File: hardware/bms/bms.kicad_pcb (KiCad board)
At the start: 4 copper layers, 120 x 45 mm, 265 parts, among them J1 Screw_Terminal_01x01, J10 Conn_01x10, J11 USB_C_Receptacle_USB2.0, J12 Conn_01x03, J13 Conn_01x07, J2 Screw_Terminal_01x01, J3 Screw_Terminal_01x01, J4 Screw_Terminal_01x01, J5 Screw_Terminal_01x01, J6 Conn_01x02, J7 Conn_01x10, J8 Conn_01x02, Q1 MMBT3904, Q2 Q_PMOS_GSD, Q3 Q_PMOS_GSD, Q4 BSZ018N04LS6ATMA1, Q5 IAUC120N04S6N006ATMA1, Q6 IAUC120N04S6N006ATMA1, Q7 BSZ018N04LS6ATMA1, Q8 BSZ018N04LS6ATMA1, Q9 BSZ018N04LS6ATMA1, SW1 SW_SPST, SW2 SW_Push, SW3 SW_Push, U1 BQ76952, U2 LM74700, U3 BQ24610, U4 LM5166X, U5 TPS62172DSG, U6 ESP32-C3-MINI-1-N4, U7 SN74LXC1T14DCKR, U8 USBLC6-2SC6

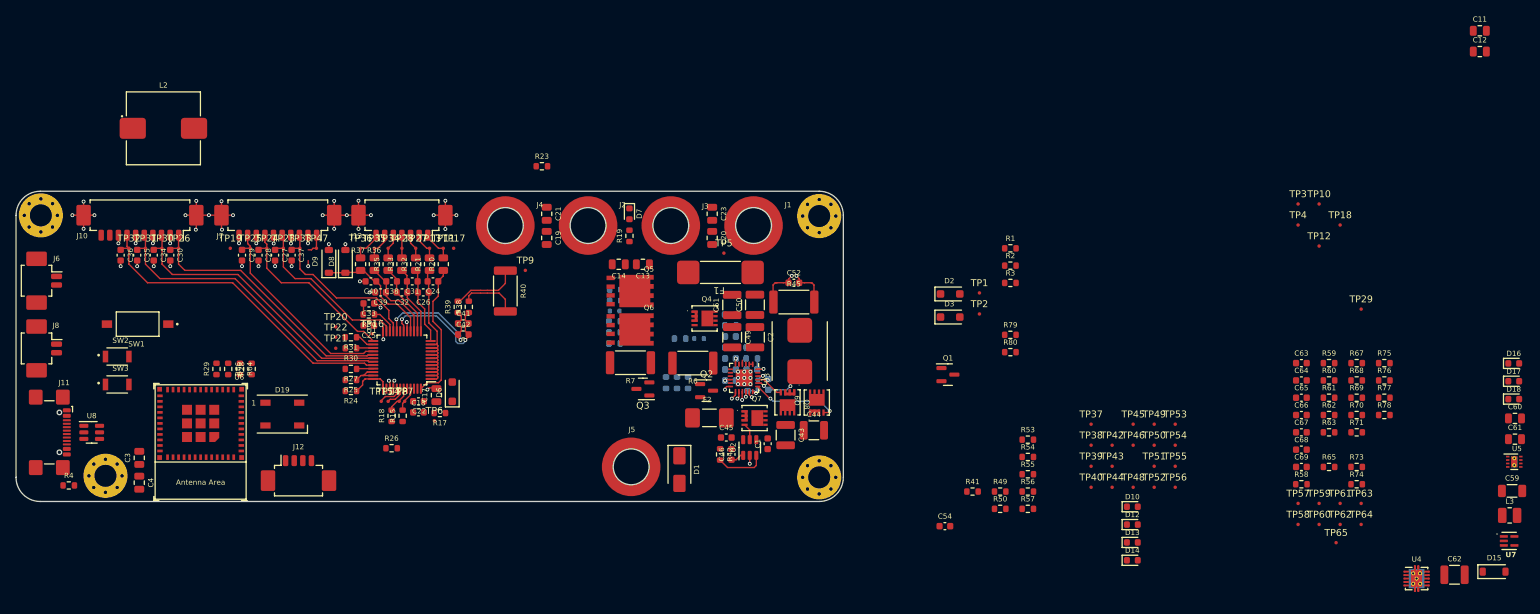
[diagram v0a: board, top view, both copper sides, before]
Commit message: Added Micro SD card circuit.
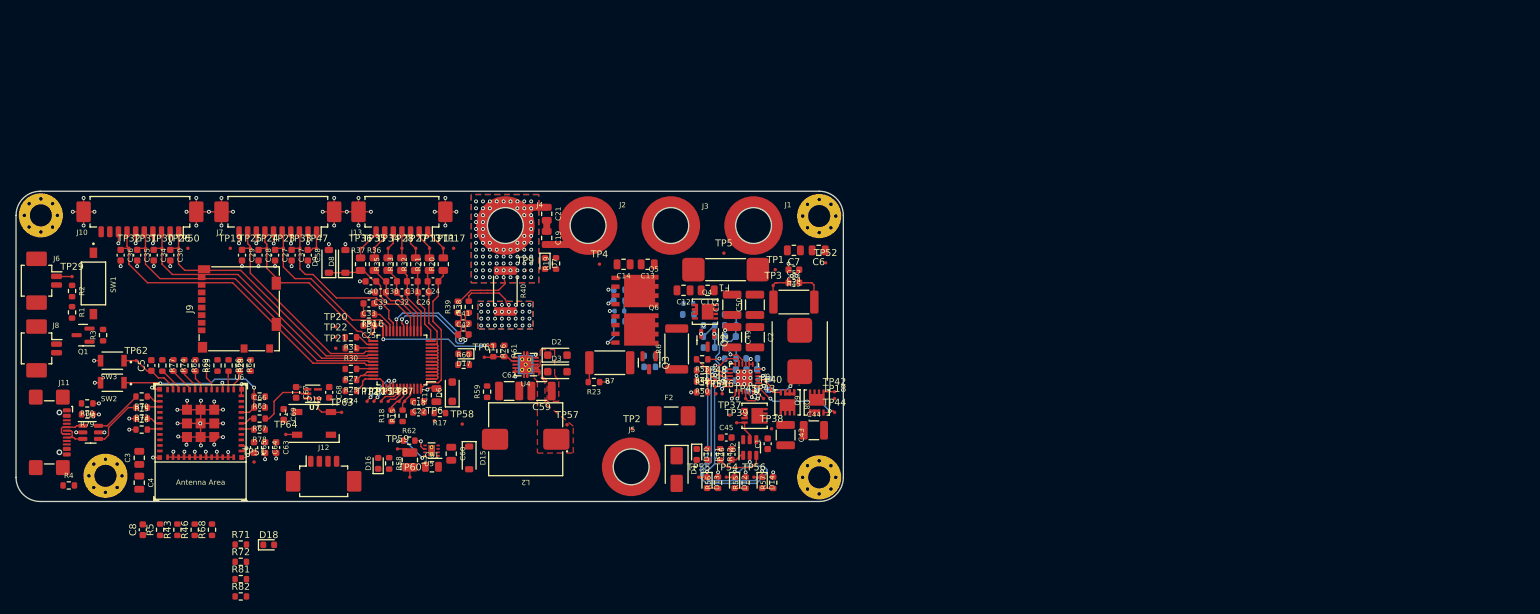
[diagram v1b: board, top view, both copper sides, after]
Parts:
- removed C20, C23: 0.1uF, Capacitor_SMD:C_0805_2012Metric
- removed TP65: TestPoint, bms:TestPoint_Pad_D0.5mm
- added C5: 0.1uF, Capacitor_SMD:C_0603_1608Metric, F.Cu at (108.4, 100.3)
- added C6: 0.1uF, Capacitor_SMD:C_0805_2012Metric, F.Cu at (205.2, 83.6)
- added C7: 0.1uF, Capacitor_SMD:C_0805_2012Metric, F.Cu at (201.6, 83.6)
- added C8: 0.1uF, Capacitor_SMD:C_0603_1608Metric, F.Cu at (107.2, 124.1)
- added J9: Micro_SD_Card_Det2, bms:microSD_HC_Molex_104031-0811, F.Cu at (121.2, 92.1)
- added R43: 0R, Resistor_SMD:R_0603_1608Metric, F.Cu at (112.2, 124.1)
- added R46: 0R, Resistor_SMD:R_0603_1608Metric, F.Cu at (114.7, 124.1)
- added R5: 0R, Resistor_SMD:R_0603_1608Metric, F.Cu at (109.7, 124.1)
- added R72: 10k, Resistor_SMD:R_0603_1608Metric, F.Cu at (121.4, 128.8)
- added R81: 10k, Resistor_SMD:R_0603_1608Metric, F.Cu at (121.4, 131.3)
- added R82: 1k, Resistor_SMD:R_0603_1608Metric, F.Cu at (121.4, 133.8)
- C58: moved to F.Cu
- C59: footprint Capacitor_SMD:C_1206_3216Metric -> Capacitor_SMD:C_1210_3225Metric
- D18: value RED -> GREEN
- R71: value 1k -> 10k
- moved TP29 187.0 mm to (96.9, 87.4)
- moved D18 181.8 mm to (125.4, 126.3)
- moved R75 180.4 mm to (107.0, 108.0)
- moved R76 180.4 mm to (107.0, 109.6)
- moved R77 177.3 mm to (110.0, 100.3), turned to -90 degrees
- moved R73 176.4 mm to (107.0, 106.4), turned to 180 degrees
- moved R70 176.3 mm to (107.0, 104.8), turned to 180 degrees
- moved TP62 176.2 mm to (106.2, 99.6)
- moved U7 174.9 mm to (131.8, 104.4)
- moved R74 172.5 mm to (111.6, 100.3), turned to -90 degrees
- moved R69 168.5 mm to (114.8, 100.3), turned to -90 degrees
- moved R68 167.4 mm to (117.2, 124.1), turned to 90 degrees
- moved R65 166.7 mm to (113.2, 100.3), turned to -90 degrees
- moved D16 165.4 mm to (141.3, 114.5), turned to 90 degrees
- moved R78 163.2 mm to (124.1, 109.6), turned to 180 degrees
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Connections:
- D18 pad 1: GND -> Net-(D18-K)
- R68 pad 2: /MCU/FAULT -> /CHG_STAT2
- R71 pad 1: Net-(D18-A) -> +3V3
- R71 pad 2: /MCU/FAULT -> Net-(J9-DAT1)
- R74 pad 1: /CHG_STAT2 -> /MCU/SCLK
- U8 pad 1: /USB_D+_CONN -> /USB_D-_CONN
- U8 pad 3: /USB_D-_CONN -> /USB_D+_CONN
- U8 pad 4: /USB_D- -> /USB_D+
- U8 pad 6: /USB_D+ -> /USB_D-
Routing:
- net GND: track 77.4 -> 147.6 mm, vias 58 -> 127
- net /CHG_STAT1: track 0.00 -> 40.0 mm, vias 0 -> 2
- net /BATTERY CHARGER/~{PG}: track 0.00 -> 30.1 mm, vias 0 -> 2
- net /MCU/EN: track 0.00 -> 24.7 mm, vias 0 -> 2
- net /BATTERY BALANCE AND MONITOR/REG18: track 1.18 -> 21.2 mm, vias 1 -> 2
- net /CHG_STAT2: track 0.00 -> 18.8 mm, vias 0 -> 2
- net /BATTERY CHARGER/VFB: track 1.10 -> 15.1 mm
- net /BATTERY CHARGER/VREF: track 2.15 -> 11.9 mm, vias 2 -> 7
- net /MCU/BOOT: track 0.00 -> 9.09 mm
- net /MCU/RGB_DIN_ESP: track 0.00 -> 8.80 mm
- net /BATTERY BALANCE AND MONITOR/PACK+: track 0.00 -> 8.53 mm, vias 0 -> 2
- net /USB_D+: track 0.00 -> 7.98 mm
- net /USB_D-: track 0.00 -> 7.24 mm
- net /BATTERY CHARGER/ISET1: track 0.00 -> 6.67 mm
- net /MCU/PG: track 0.00 -> 5.83 mm, vias 0 -> 2
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- added copper zone on B.Cu, net /BATTERY BALANCE AND MONITOR/PACK-
- added copper zone on F.Cu, net /BATTERY BALANCE AND MONITOR/PACK-
- added copper zone on In1.Cu, net /BATTERY BALANCE AND MONITOR/PACK-
- added copper zone on In2.Cu, net /BATTERY BALANCE AND MONITOR/PACK-
- added copper zone on F.Cu, net /MCU/5V_SW
- added copper zone on F.Cu, net /MCU/MCU_VIN
- added copper zone on B.Cu, net GND
- added copper zone on F.Cu, net GND
- added copper zone on In1.Cu, net GND
- added copper zone on In2.Cu, net GND

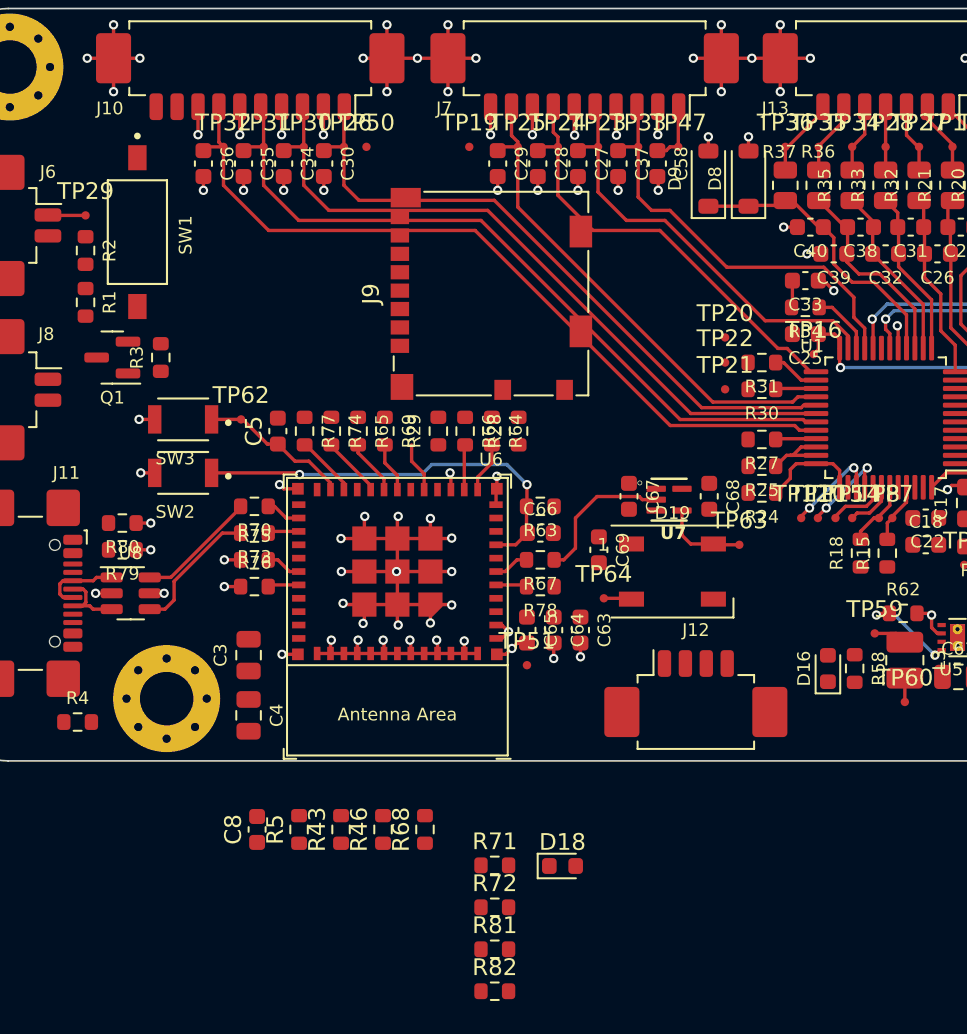
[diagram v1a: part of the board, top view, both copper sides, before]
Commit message: Layout complete! MicroSD card fits just fine
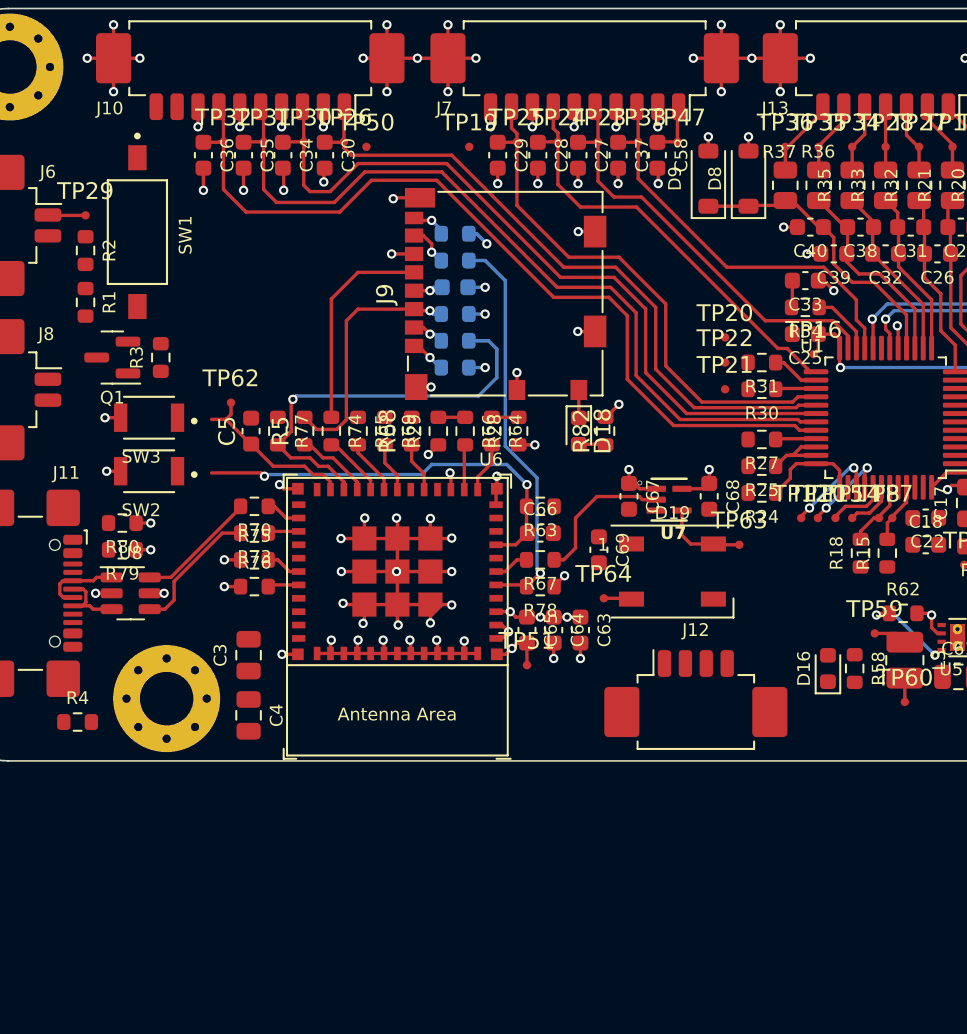
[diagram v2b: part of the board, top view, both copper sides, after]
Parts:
- C8, R43, R46, R71, R72, R81: moved to B.Cu
- moved R71 37.8 mm to (119.0, 88.5), turned to 180 degrees
- moved R72 35.6 mm to (119.0, 93.3), turned to 180 degrees
- moved R81 34.9 mm to (119.0, 96.5), turned to 180 degrees
- moved C8 34.5 mm to (119.0, 91.7), turned to 0 degrees
- moved R46 34.3 mm to (119.0, 90.1), turned to 0 degrees
- moved R82 34.1 mm to (128.0, 100.3), turned to 90 degrees
- moved R43 30.0 mm to (119.0, 94.9), turned to 180 degrees
- moved D18 26.0 mm to (126.4, 100.3), turned to -90 degrees
- moved R68 23.8 mm to (116.4, 100.3)
- moved R5 23.8 mm to (110.0, 100.3)
- moved SW2 2.04 mm to (100.7, 102.7)
- moved SW3 2.04 mm to (100.7, 99.5)
- moved C5 1.60 mm to (106.8, 100.3)
- moved R77 1.60 mm to (108.4, 100.3)
- moved TP62 1.17 mm to (105.6, 98.6)
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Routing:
- net /MCU/GPIO2: track 1.87 -> 24.1 mm, vias 0 -> 1
- net /MCU/GPIO8: track 3.69 -> 24.7 mm, vias 0 -> 1
- net +3V3: track 3.84 -> 21.3 mm, vias 1 -> 13
- net /MCU/MOSI: track 0.00 -> 15.0 mm, vias 0 -> 1
- net /MCU/SCLK: track 0.00 -> 12.7 mm
- net GND: track 147.6 -> 154.6 mm, vias 127 -> 134
- net /MCU/GPIO7: track 0.00 -> 4.52 mm
- net /THERM_7: track 47.1 -> 51.2 mm
- net /THERM_6: track 44.5 -> 48.5 mm
- net /THERM_5: track 41.8 -> 45.7 mm
- net +5V: track 0.00 -> 2.59 mm, vias 0 -> 1
- net /MCU/MISO: track 0.00 -> 2.53 mm, vias 0 -> 1
- net Net-(J9-DAT2): track 0.00 -> 2.16 mm, vias 0 -> 1
- net Net-(J9-DAT1): track 0.00 -> 2.15 mm, vias 0 -> 1
- net /THERM_3: track 29.7 -> 31.8 mm
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
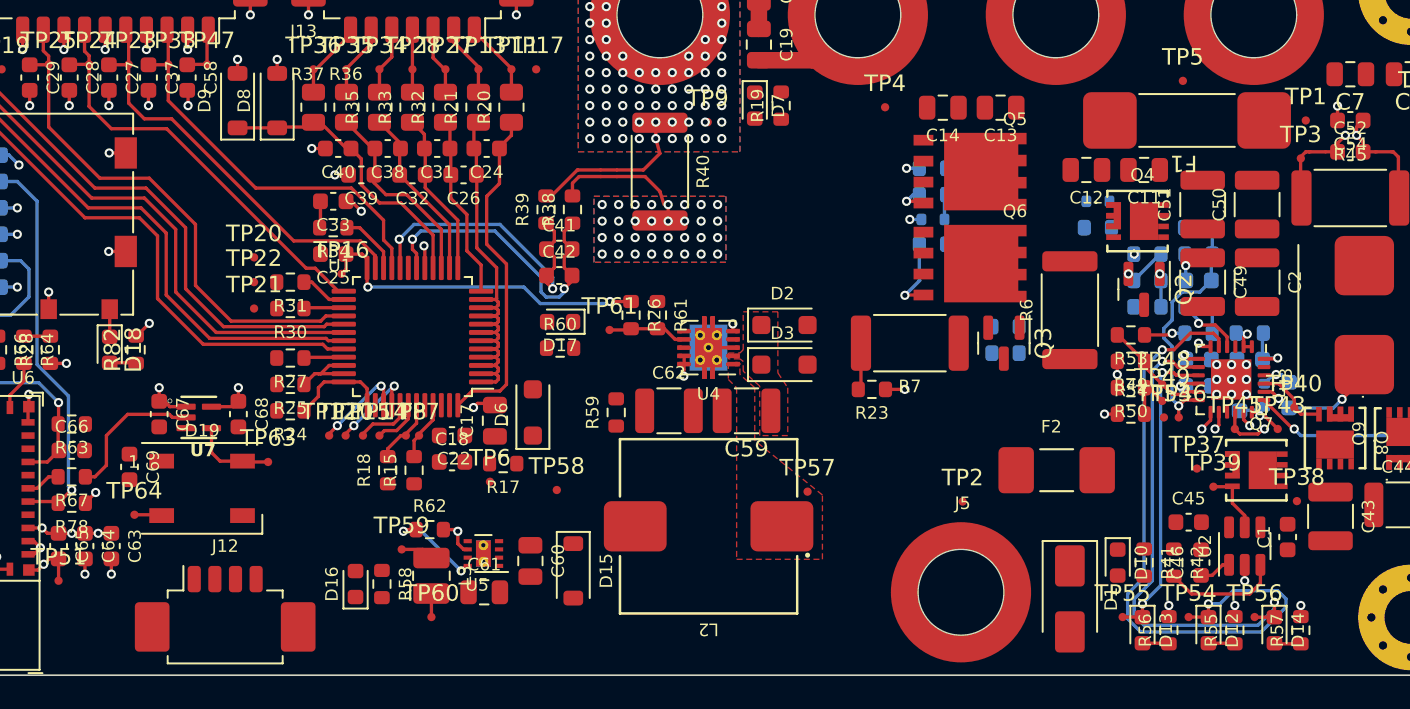
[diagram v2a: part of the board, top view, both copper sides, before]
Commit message: Modified layout to fit inside enclosure and around penetrators. Routing time!
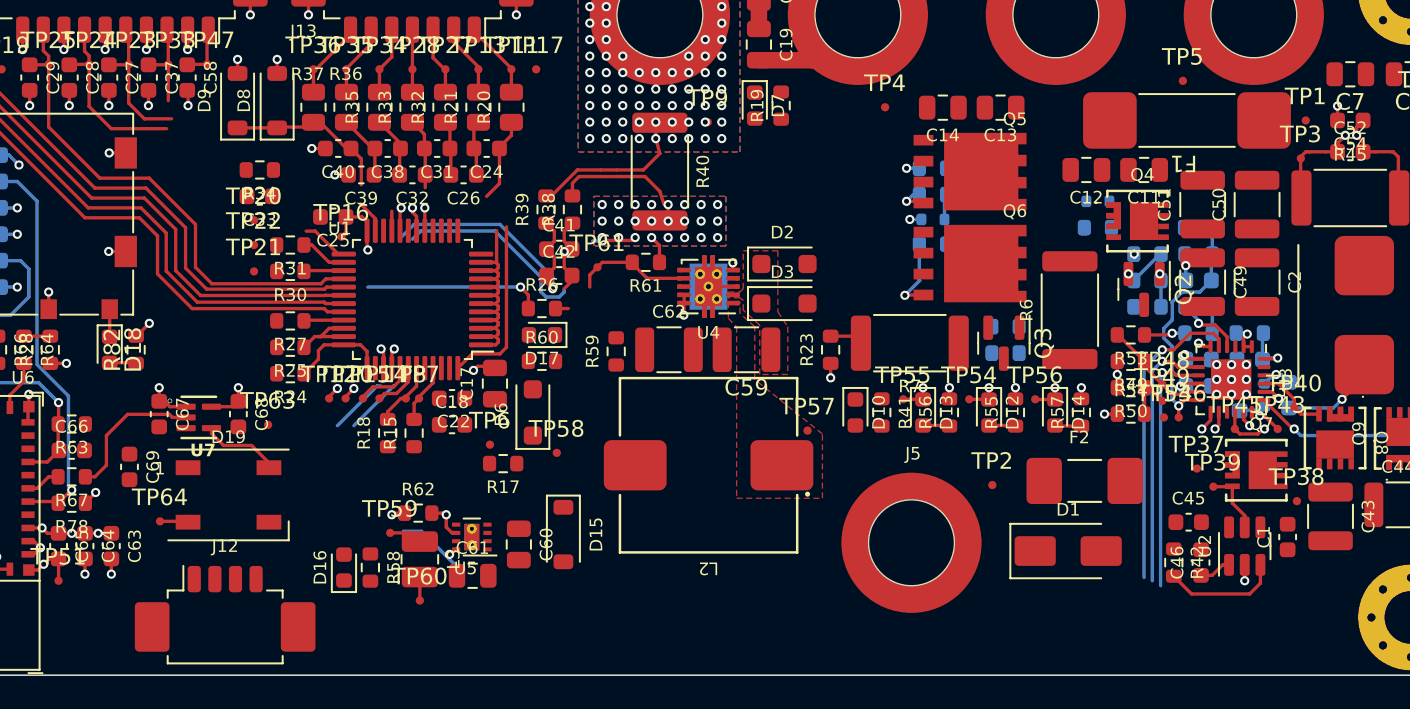
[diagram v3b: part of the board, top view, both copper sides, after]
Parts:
- moved D12 18.7 mm to (179.7, 104.1)
- moved D13 18.7 mm to (175.7, 104.1)
- moved D14 18.7 mm to (183.7, 104.1)
- moved TP54 18.7 mm to (178.5, 103.3)
- moved TP55 18.7 mm to (174.5, 103.3)
- moved TP56 18.7 mm to (182.5, 103.3)
- moved R55 18.7 mm to (181.3, 104.1)
- moved R56 18.7 mm to (177.3, 104.1)
- moved R57 18.7 mm to (185.3, 104.1)
- moved D10 18.3 mm to (171.6, 104.1)
- moved R41 18.3 mm to (173.2, 104.1)
- moved R34 5.66 mm to (135.5, 89.4)
- moved R26 5.41 mm to (152.6, 97.8), turned to 0 degrees
- moved C33 4.46 mm to (135.5, 91.0)
- moved J5 4.24 mm to (175.0, 112.0)
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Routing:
- net /CHG_STAT1: track 40.0 -> 20.6 mm
- net /THERM_0: track 24.2 -> 6.23 mm
- net /THERM_1: track 24.8 -> 10.2 mm
- net /BATTERY CHARGER/~{PG}: track 30.1 -> 17.8 mm
- net /THERM_2: track 25.9 -> 13.9 mm
- net /BATTERY BALANCE AND MONITOR/VC1: track 12.1 -> 4.00 mm
- net /BATTERY BALANCE AND MONITOR/VC4: track 11.1 -> 3.32 mm
- net /BATTERY BALANCE AND MONITOR/VC0: track 17.7 -> 10.1 mm
- net /BATTERY BALANCE AND MONITOR/VC2: track 10.6 -> 3.74 mm
- net /BATTERY BALANCE AND MONITOR/VC15: track 27.5 -> 21.4 mm
- net /BATTERY BALANCE AND MONITOR/REG18: track 21.2 -> 15.4 mm
- net /BATTERY BALANCE AND MONITOR/VC3: track 9.96 -> 4.28 mm
- net /BATTERY BALANCE AND MONITOR/VC16: track 20.5 -> 15.9 mm
- net /BATTERY BALANCE AND MONITOR/TS2: track 3.81 -> 0.00 mm
- net GND: track 154.6 -> 157.7 mm, vias 134 -> 126
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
